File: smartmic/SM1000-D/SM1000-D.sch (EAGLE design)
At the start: 196 parts, among them CN1 HDR100-3, CN10 ST-3509, CN11 HDR100-3, CN12 HRS-A3C-16DA, CN2 JS-MU3-002, CN3 DS-0518, CN4 RJ-45, CN5 ST-3509, CN6 ST-3509, CN7 ST-3509, CN8 ST-3509, CN9 ST-3509, J1 JMP-2PIN, J3 JMP-2PIN, J4 JMP-2PIN, P1 TPAD50, P10 TPAD50, P11 TPAD50, P12 TPAD50, P13 TPAD50, P14 TPAD50, P16 TPAD50, P18 TPAD50, P19 TPAD50, P2 TPAD50, P20 TPAD50, P3 TPAD50, P4 TPAD50, P5 TPAD50, P6 TPAD50, P7 TPAD50, P8 TPAD50, P9 TPAD50, SW1 SW-SPDT-8US8WR2C2M7RES, SW2 TS-026, SW3 DPDT, SW4 TS-026, SW5 TS-02B, T1 SM-LP-5001, T2 SM-LP-5001, U1 STM32F405VGT6, U2 LD3985M33R, U3 STMPS2141, U4 EMIF02-USB03F2, U5 TPS54329E, U6 LMV341, U7 LMV341, U8 LM386M-1, U9 LMV341

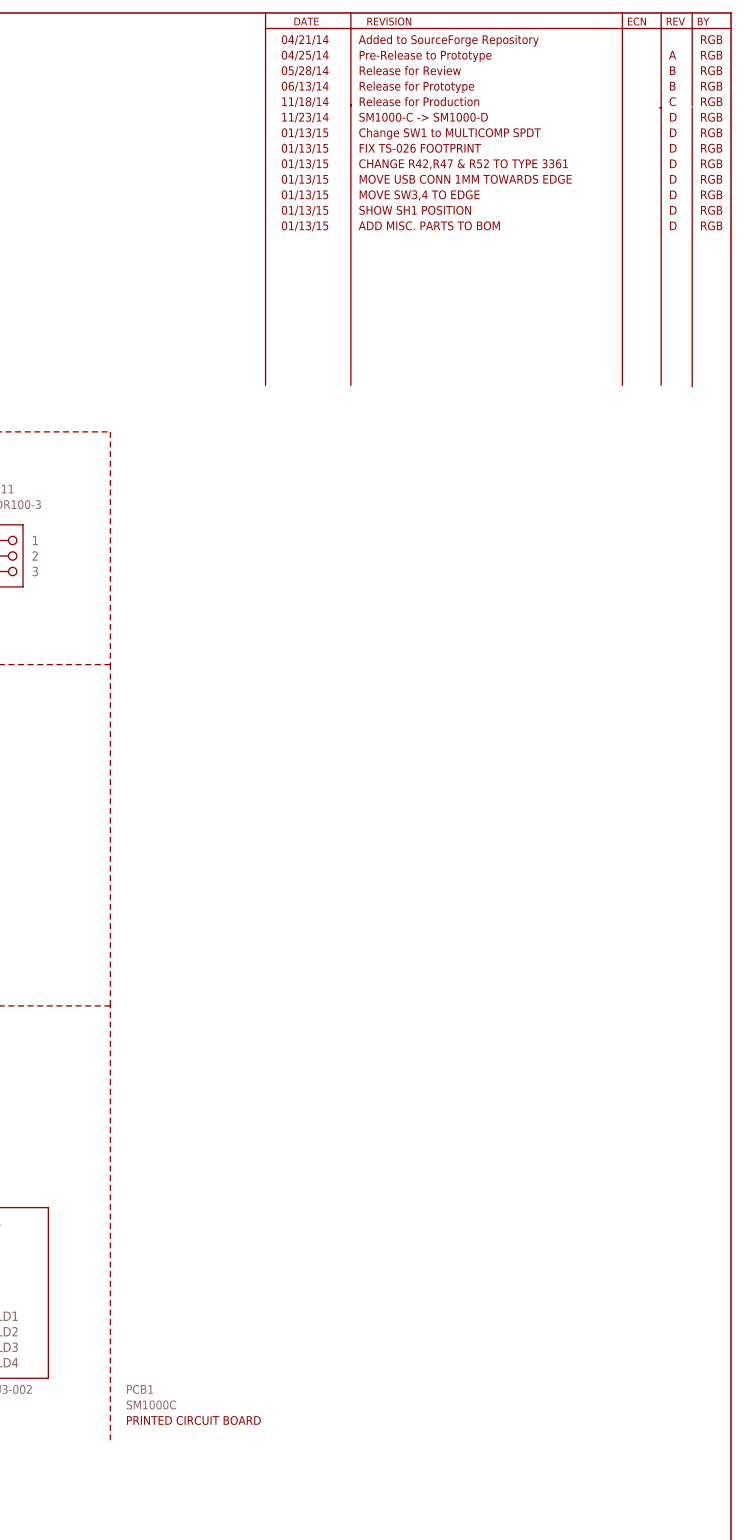
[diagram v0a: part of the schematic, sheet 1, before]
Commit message: Move Top Assembly items to separate drawing
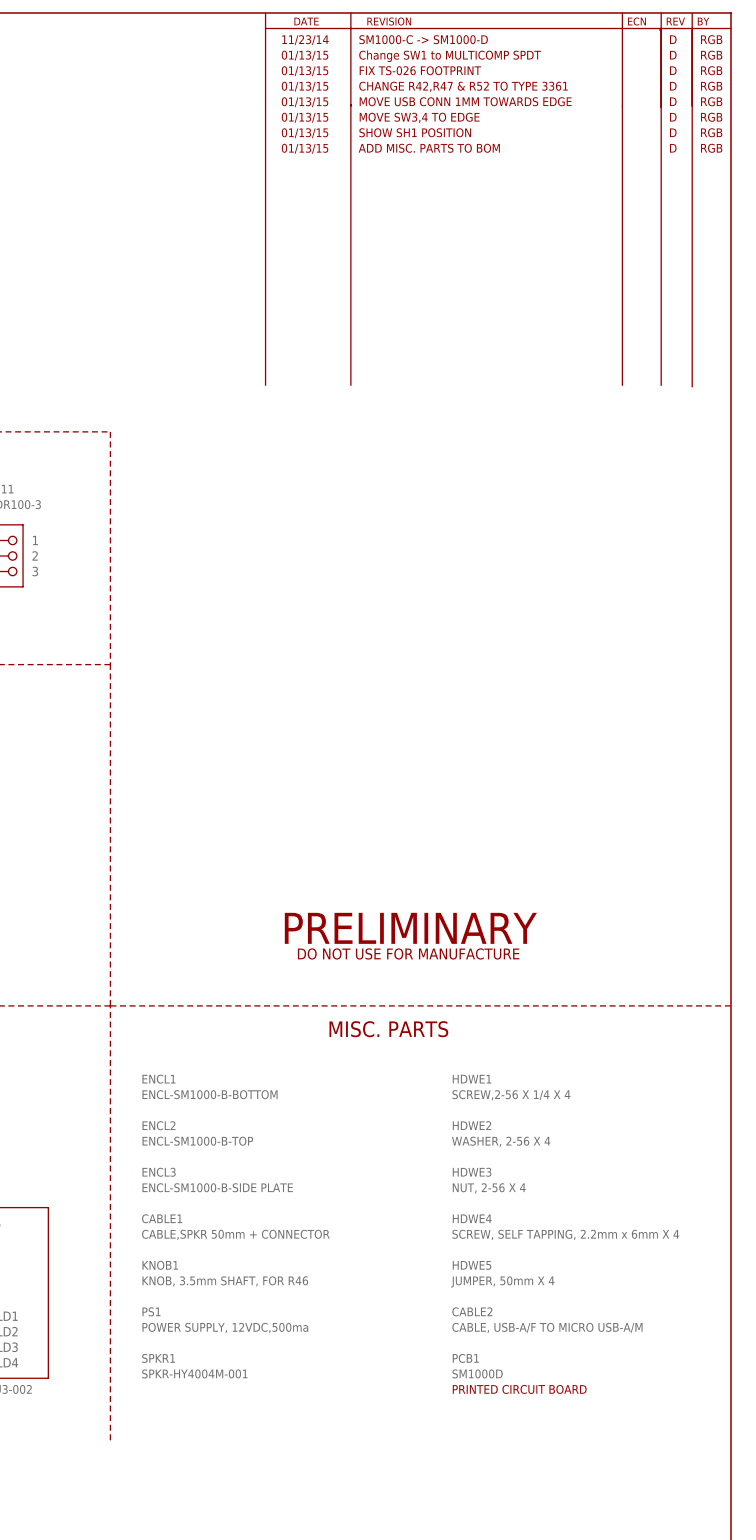
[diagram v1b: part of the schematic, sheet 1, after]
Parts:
- added CABLE1: CABLE,SPKR 50mm + CONNECTOR, _RoweTel:CABLE
- added CABLE2: CABLE, USB-A/F TO MICRO USB-A/M, _RoweTel:CABLE
- added ENCL1: ENCL-SM1000-B-BOTTOM, _RoweTel:ENCL
- added ENCL2: ENCL-SM1000-B-TOP, _RoweTel:ENCL
- added ENCL3: ENCL-SM1000-B-SIDE PLATE, _RoweTel:ENCL
- added HDWE1: SCREW,2-56 X 1/4 X 4, _RoweTel:HDWE
- added HDWE2: WASHER, 2-56 X 4, _RoweTel:HDWE
- added HDWE3: NUT, 2-56 X 4, _RoweTel:HDWE
- added HDWE4: SCREW, SELF TAPPING, 2.2mm x 6mm X 4, _RoweTel:HDWE
- added HDWE5: JUMPER, 50mm X 4, _RoweTel:HDWE
- added KNOB1: KNOB, 3.5mm SHAFT, FOR R46, _RoweTel:KNOB
- added PS1: POWER SUPPLY, 12VDC,500ma, _RoweTel:PS
- added U$5: PRELIMINARY, _RoweTel:PRELIMINARY
- PCB1: value SM1000C -> SM1000D
- R42: value 500K,POT -> 500K,TrimPOT
- R47: value 500,POT -> 500,TrimPOT
- R52: value 1K,POT -> 1K,TrimPOT
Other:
- note added: "MISC. PARTS"
- note removed: "04/21/14"
- note removed: "04/25/14"
- note removed: "05/28/14"
- note removed: "06/13/14"
- note removed: "11/18/14"
- note removed: "A"
- note removed: "Added to SourceForge Repository"
- note removed: "B"
- note removed: "C"
- note removed: "Pre-Release to Prototype"
- note removed: "Release for Production"
- note removed: "Release for Prototype"
- note removed: "Release for Review"
- moved on the sheet: PCB1

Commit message: Production Release of SM1000-D PCB files
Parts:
- removed CABLE1: CABLE,SPKR 50mm + CONNECTOR, _RoweTel:CABLE
- removed CABLE2: CABLE, USB-A/F TO MICRO USB-A/M, _RoweTel:CABLE
- removed ENCL1: ENCL-SM1000-B-BOTTOM, _RoweTel:ENCL
- removed ENCL2: ENCL-SM1000-B-TOP, _RoweTel:ENCL
- removed ENCL3: ENCL-SM1000-B-SIDE PLATE, _RoweTel:ENCL
- removed HDWE1: SCREW,2-56 X 1/4 X 4, _RoweTel:HDWE
- removed HDWE2: WASHER, 2-56 X 4, _RoweTel:HDWE
- removed HDWE3: NUT, 2-56 X 4, _RoweTel:HDWE
- removed HDWE4: SCREW, SELF TAPPING, 2.2mm x 6mm X 4, _RoweTel:HDWE
- removed HDWE5: JUMPER, 50mm X 4, _RoweTel:HDWE
- removed KNOB1: KNOB, 3.5mm SHAFT, FOR R46, _RoweTel:KNOB
- removed PS1: POWER SUPPLY, 12VDC,500ma, _RoweTel:PS
- removed U$5: PRELIMINARY, _RoweTel:PRELIMINARY
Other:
- note added: "01-23-15"
- note added: "01/23/15"
- note added: "RELEASE REV. D TO PRODUCTION"
- note added: "RELEASE REV. D TO PRODUCTION."
- moved on the sheet: PCB1
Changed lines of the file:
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@@
 <part name="LED8" library="_RoweTel" deviceset="SML-LX0603SRW" device="" value="SML-LX0603SRW-TR"/>
 <part name="LED5" library="_RoweTel" deviceset="SML-LX0603SRW" device="" value="SML-LX0603SRW-TR"/>
-<part name="U$5" library="_RoweTel" deviceset="PRELIMINARY" device=""/>
-<part name="ENCL1" library="_RoweTel" deviceset="ENCL" device="" value="ENCL-SM1000-B-BOTTOM"/>
-<part name="ENCL2" library="_RoweTel" deviceset="ENCL" device="" value="ENCL-SM1000-B-TOP"/>
-<part name="ENCL3" library="_RoweTel" deviceset="ENCL" device="" value="ENCL-SM1000-B-SIDE PLATE"/>
-<part name="HDWE1" library="_RoweTel" deviceset="HDWE" device="" value="SCREW,2-56 X 1/4 X 4"/>
-<part name="HDWE2" library="_RoweTel" deviceset="HDWE" device="" value="WASHER, 2-56 X 4"/>
-<part name="HDWE3" library="_RoweTel" deviceset="HDWE" device="" value="NUT, 2-56 X 4"/>
-<part name="HDWE4" library="_RoweTel" deviceset="HDWE" device="" value="SCREW, SELF TAPPING, 2.2mm x 6mm X 4"/>
-<part name="HDWE5" library="_RoweTel" deviceset="HDWE" device="" value="JUMPER, 50mm X 4"/>
-<part name="CABLE1" library="_RoweTel" deviceset="CABLE" device="" value="CABLE,SPKR 50mm + CONNECTOR"/>
-<part name="KNOB1" library="_RoweTel" deviceset="KNOB" device="" value="KNOB, 3.5mm SHAFT, FOR R46"/>
-<part name="PS1" library="_RoweTel" deviceset="PS" device="" value="POWER SUPPLY, 12VDC,500ma"/>
-<part name="CABLE2" library="_RoweTel" deviceset="CABLE" device="" value="CABLE, USB-A/F TO MICRO USB-A/M"/>
 <part name="SPKR1" library="_RoweTel" deviceset="SPKR-HY4004M-001" device=""/>
 </parts>
@@
 <wire x1="185.42" y1="172.72" x2="185.42" y2="116.84" width="0.1524" layer="94" style="longdash"/>
 <wire x1="185.42" y1="116.84" x2="185.42" y2="0" width="0.1524" layer="94" style="longdash"/>
-<wire x1="330.2" y1="45.72" x2="330.2" y2="116.84" width="0.1524" layer="94" style="longdash"/>
+<wire x1="330.2" y1="45.72" x2="330.2" y2="71.12" width="0.1524" layer="94" style="longdash"/>
+<wire x1="330.2" y1="71.12" x2="330.2" y2="116.84" width="0.1524" layer="94" style="longdash"/>
 <wire x1="330.2" y1="116.84" x2="185.42" y2="116.84" width="0.1524" layer="94" style="longdash"/>
 <wire x1="330.2" y1="116.84" x2="330.2" y2="172.72" width="0.1524" layer="94" style="longdash"/>
@@
 <text x="421.64" y="256.54" size="1.4224" layer="94" ratio="10">D</text>
 <text x="426.72" y="256.54" size="1.4224" layer="94" ratio="10">RGB</text>
-<wire x1="330.2" y1="116.84" x2="431.8" y2="116.84" width="0.1524" layer="94" style="longdash"/>
-<text x="365.76" y="111.76" size="2.54" layer="94" ratio="10">MISC. PARTS</text>
+<text x="363.22" y="60.96" size="2.54" layer="94" ratio="10">MISC. PARTS</text>
+<text x="370.84" y="254" size="1.4224" layer="94" ratio="10">RELEASE REV. D TO PRODUCTION</text>
+<text x="358.14" y="254" size="1.4224" layer="94" ratio="10">01-23-15</text>
+<text x="421.64" y="254" size="1.4224" layer="94" ratio="10">D</text>
+<text x="426.72" y="254" size="1.4224" layer="94" ratio="10">RGB</text>
+<wire x1="330.2" y1="71.12" x2="431.8" y2="71.12" width="0.1524" layer="94" style="longdash"/>
 </plain>
 <instances>
@@
 <instance part="B-FRAME2" gate="G$2" x="330.2" y="0"/>
 <instance part="B-FRAME2" gate="G$3" x="358.14" y="279.4"/>
-<instance part="PCB1" gate="G$1" x="386.08" y="53.34" smashed="yes">
-<attribute name="NAME" x="386.08" y="58.42" size="1.4224" layer="95" ratio="9"/>
-<attribute name="VALUE" x="386.08" y="55.88" size="1.4224" layer="95" ratio="9"/>
+<instance part="PCB1" gate="G$1" x="388.62" y="48.26" smashed="yes">
+<attribute name="NAME" x="388.62" y="53.34" size="1.4224" layer="95" ratio="9"/>
+<attribute name="VALUE" x="388.62" y="50.8" size="1.4224" layer="95" ratio="9"/>
 </instance>
 <instance part="V1" gate="GND" x="121.92" y="10.16"/>
@@
 <attribute name="VALUE" x="289.56" y="132.08" size="1.4224" layer="96" ratio="9"/>
 </instance>
-<instance part="U$5" gate="G$1" x="358.14" y="127"/>
-<instance part="ENCL1" gate="G$1" x="335.28" y="104.14"/>
-<instance part="ENCL2" gate="G$1" x="335.28" y="96.52"/>
-<instance part="ENCL3" gate="G$1" x="335.28" y="88.9"/>
-<instance part="HDWE1" gate="G$1" x="386.08" y="104.14"/>
-<instance part="HDWE2" gate="G$1" x="386.08" y="96.52"/>
-<instance part="HDWE3" gate="G$1" x="386.08" y="88.9"/>
-<instance part="HDWE4" gate="G$1" x="386.08" y="81.28"/>
-<instance part="HDWE5" gate="G$1" x="386.08" y="73.66"/>
-<instance part="CABLE1" gate="G$1" x="335.28" y="81.28"/>
-<instance part="KNOB1" gate="G$1" x="335.28" y="73.66"/>
-<instance part="PS1" gate="G$1" x="335.28" y="66.04"/>
-<instance part="CABLE2" gate="G$1" x="386.08" y="66.04"/>
-<instance part="SPKR1" gate="G$1" x="335.28" y="58.42" smashed="yes">
-<attribute name="NAME" x="335.28" y="58.42" size="1.4224" layer="95" ratio="10"/>
-<attribute name="VALUE" x="335.28" y="55.88" size="1.4224" layer="95" ratio="10"/>
+<instance part="SPKR1" gate="G$1" x="337.82" y="53.34" smashed="yes">
+<attribute name="NAME" x="337.82" y="53.34" size="1.4224" layer="95" ratio="10"/>
+<attribute name="VALUE" x="337.82" y="50.8" size="1.4224" layer="95" ratio="10"/>
 </instance>
 </instances>
@@
 <text x="419.1" y="274.32" size="1.4224" layer="94" ratio="10">D</text>
 <text x="424.18" y="274.32" size="1.4224" layer="94" ratio="10">RGB</text>
+<text x="355.6" y="271.78" size="1.4224" layer="94" ratio="10">01/23/15</text>
+<text x="368.3" y="271.78" size="1.4224" layer="94" ratio="10">RELEASE REV. D TO PRODUCTION.</text>
+<text x="419.1" y="271.78" size="1.4224" layer="94" ratio="10">D</text>
+<text x="424.18" y="271.78" size="1.4224" layer="94" ratio="10">RGB</text>
 </plain>
 <instances>
